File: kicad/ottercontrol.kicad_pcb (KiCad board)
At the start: 2 copper layers, 97.8 x 52.1 mm, 114 parts, among them IC1 MAX485, IC2 USBLC6-4, IC3 USBLC6-2SC6, J1 USB_B_Micro, P1 Conn_01x02, Q1 Q_PMOS_GSD, Q2 IRF3205, Q3 IRF3205, Q4 IRF3205, Q5 IRF3205, Q6 IRF3205, Q7 IRF3205, U1 STM32F303CBT6, U2 MAX3051, U3 MIC4605, U4 MIC4605, U5 MIC4605, U6 XL7015, U7 ACT4088, U8 MIC5504-3.3YM5, X1 programmer, X2 Conn_01x08, X3 Conn_01x05, Y1 16MHz

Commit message: placed and routed; preliminary finished
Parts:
- added GND1: Conn_01x01, TestPoint:TestPoint_THTPad_4.0x4.0mm_Drill2.0mm, F.Cu at (140.3, 80.0)
- added R48: 0, Resistor_SMD:R_0603_1608Metric, F.Cu at (134.0, 69.2)
- added VDC1: Conn_01x01, TestPoint:TestPoint_THTPad_4.0x4.0mm_Drill2.0mm, F.Cu at (62.9, 80.0)
- added VDC2: Conn_01x01, TestPoint:TestPoint_THTPad_4.0x4.0mm_Drill2.0mm, F.Cu at (57.1, 80.0)
- X1: footprint Connector_PinHeader_2.54mm:PinHeader_2x03_P2.54mm_Vertical -> Connector:Tag-Connect_TC2030-IDC-NL_2x03_P1.27mm_Vertical
- X2: footprint Connector_JST:JST_GH_SM08B-GHS-TB_1x08-1MP_P1.25mm_Horizontal -> Connector_Molex:Molex_PicoBlade_53261-0871_1x08-1MP_P1.25mm_Horizontal
- X3: footprint Connector_JST:JST_GH_SM05B-GHS-TB_1x05-1MP_P1.25mm_Horizontal -> Connector_Molex:Molex_PicoBlade_53261-0571_1x05-1MP_P1.25mm_Horizontal
- moved C3 25.6 mm to (116.2, 66.0), turned to 90 degrees
- moved C11 12.1 mm to (104.8, 64.8), turned to 270 degrees
- moved C12 11.5 mm to (94.0, 64.8), turned to 270 degrees
- moved C13 10.9 mm to (83.2, 64.8), turned to 270 degrees
- moved R27 6.29 mm to (89.5, 47.6)
- moved R43 5.99 mm to (108.0, 73.0)
- moved X2 5.99 mm to (91.4, 81.9)
- moved R14 5.85 mm to (119.4, 79.4)
- moved R3 5.85 mm to (119.4, 81.9)
- moved X3 5.46 mm to (107.3, 81.9)
- moved LED1 5.46 mm to (117.5, 81.9)
- moved R2 5.12 mm to (115.6, 81.9), turned to 270 degrees
- moved R11 5.12 mm to (120.7, 78.1)
- moved U2 4.96 mm to (95.2, 74.3)
- moved IC1 4.96 mm to (88.9, 74.3)
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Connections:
- net Net-(R15-Pad2) renamed /Phase Driver 1/HO
- net Net-(R16-Pad2) renamed /Phase Driver 2/HO
- net Net-(R17-Pad2) renamed /Phase Driver 3/HO
- net Net-(R18-Pad2) renamed /Phase Driver 1/LO
- net Net-(R19-Pad2) renamed /Phase Driver 2/LO
- net Net-(R20-Pad2) renamed /Phase Driver 3/LO
- C5 pad 1: +5V -> +3V3
- IC1 pad 4: /RS458_TX -> /RS485_TX
- IC2 pad 5: +3V3 -> +5V
- IC3 pad 4: Net-(IC3-Pad4) -> Net-(IC3-Pad3)
- IC3 pad 6: Net-(IC3-Pad6) -> Net-(IC3-Pad1)
- R11 pad 1: Net-(IC3-Pad6) -> Net-(IC3-Pad1)
- R12 pad 2: Net-(IC3-Pad4) -> Net-(IC3-Pad3)
- R14 pad 2: Net-(IC3-Pad4) -> Net-(IC3-Pad3)
- U1 pad 21: /RS458_TX -> /RS485_TX
- U2 pad 3: +5V -> +3V3
- X3 pad 5: +3V3 -> +5V
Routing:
- net +12V: track 0.00 -> 67.1 mm, vias 0 -> 9
- net +5V: track 0.00 -> 66.8 mm
- net +3V3: track 0.00 -> 66.0 mm, vias 0 -> 18
- net /VSENS3: track 0.00 -> 52.0 mm, vias 0 -> 2
- net GND: track 0.00 -> 48.3 mm, vias 0 -> 26
- net /RS485_RX: track 0.00 -> 43.9 mm, vias 0 -> 2
- net Net-(Q7-Pad3): track 0.00 -> 41.3 mm, vias 0 -> 3
- net /RS485_DE: track 0.00 -> 40.7 mm, vias 0 -> 2
- net /Phase Driver 1/PHASE: track 0.00 -> 40.1 mm, vias 0 -> 74
- net /CAN_EN: track 0.00 -> 39.5 mm, vias 0 -> 2
- net /CAN_TX: track 0.00 -> 39.3 mm, vias 0 -> 3
- net /VSENS1: track 0.00 -> 39.1 mm, vias 0 -> 3
- net /PWML3: track 0.00 -> 37.6 mm, vias 0 -> 2
- net +VDC: track 0.00 -> 37.6 mm, vias 0 -> 74
- net /VSENS2: track 0.00 -> 37.5 mm, vias 0 -> 3
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- added copper zone on F.Cu, net +12V
- added copper zone on In1.Cu, net +12V
- added copper zone on In1.Cu, net +3V3
- added copper zone on B.Cu, net +VDC
- added copper zone on F.Cu, net +VDC
- added copper zone on In1.Cu, net +VDC
- added copper zone on B.Cu, net /Phase Driver 1/PHASE
- added copper zone on F.Cu, net /Phase Driver 1/PHASE
- added copper zone on B.Cu, net /Phase Driver 2/PHASE
- added copper zone on F.Cu, net /Phase Driver 2/PHASE
- added copper zone on B.Cu, net /Phase Driver 3/PHASE
- added copper zone on F.Cu, net /Phase Driver 3/PHASE
- added copper zone on F.Cu, net GND
- added copper zone on In2.Cu, net GND
- added copper zone on B.Cu, net GNDPWR
- added copper zone on F.Cu, net GNDPWR
- added copper zone on In2.Cu, net GNDPWR
- added copper zone on F.Cu, net Net-(D9-Pad1)
- added copper zone on F.Cu, net Net-(Q5-Pad3)
- added copper zone on F.Cu, net Net-(Q6-Pad3)
- added copper zone on F.Cu, net Net-(Q7-Pad3)
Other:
- board size 97.8 x 52.1 mm -> 94 x 47 mm
- copper layers 2 -> 4
- net class 0.3mm added: clearance 0.2, trace_width 0.3, via_dia 0.8, via_drill 0.4
- net class 0.5mm added: clearance 0.2, trace_width 0.5, via_dia 0.8, via_drill 0.4
- net class 0.6mm added: clearance 0.2, trace_width 0.6, via_dia 0.8, via_drill 0.4
- net class 1.0mm added: clearance 0.2, trace_width 1, via_dia 1, via_drill 0.5
- net class Default: trace_width 0.25 -> 0.15; via_dia 0.8 -> 0.5; via_drill 0.4 -> 0.3
- net class High Power added: clearance 0.2, trace_width 0.8, via_dia 0.8, via_drill 0.4
- rule trace_min: 0.2 -> 0.15
- rule via_min_drill: 0.3 -> 0.25
- rule via_min_size: 0.4 -> 0.5

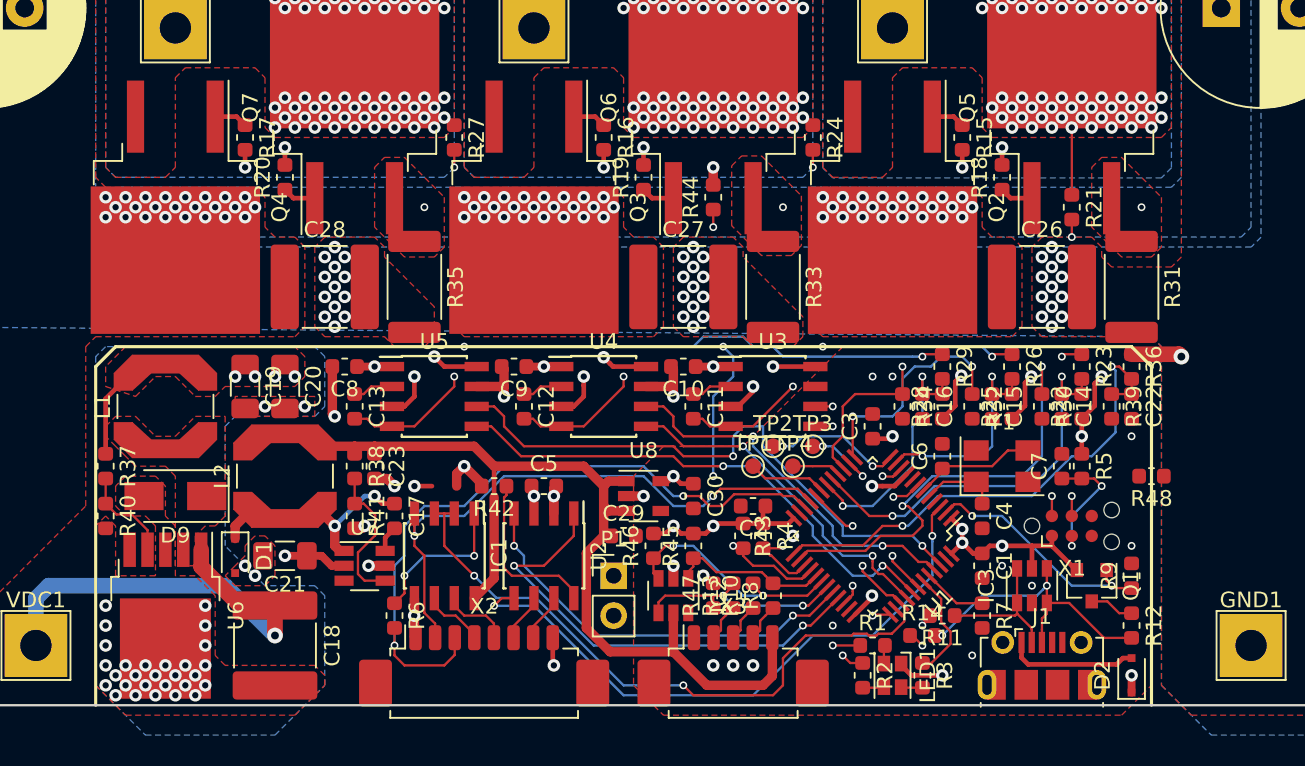
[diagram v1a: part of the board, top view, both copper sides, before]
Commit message: made footprint fot mosfets hybrid for TO220 and D2PAK; added jumper instead of 0 Ohm resistor
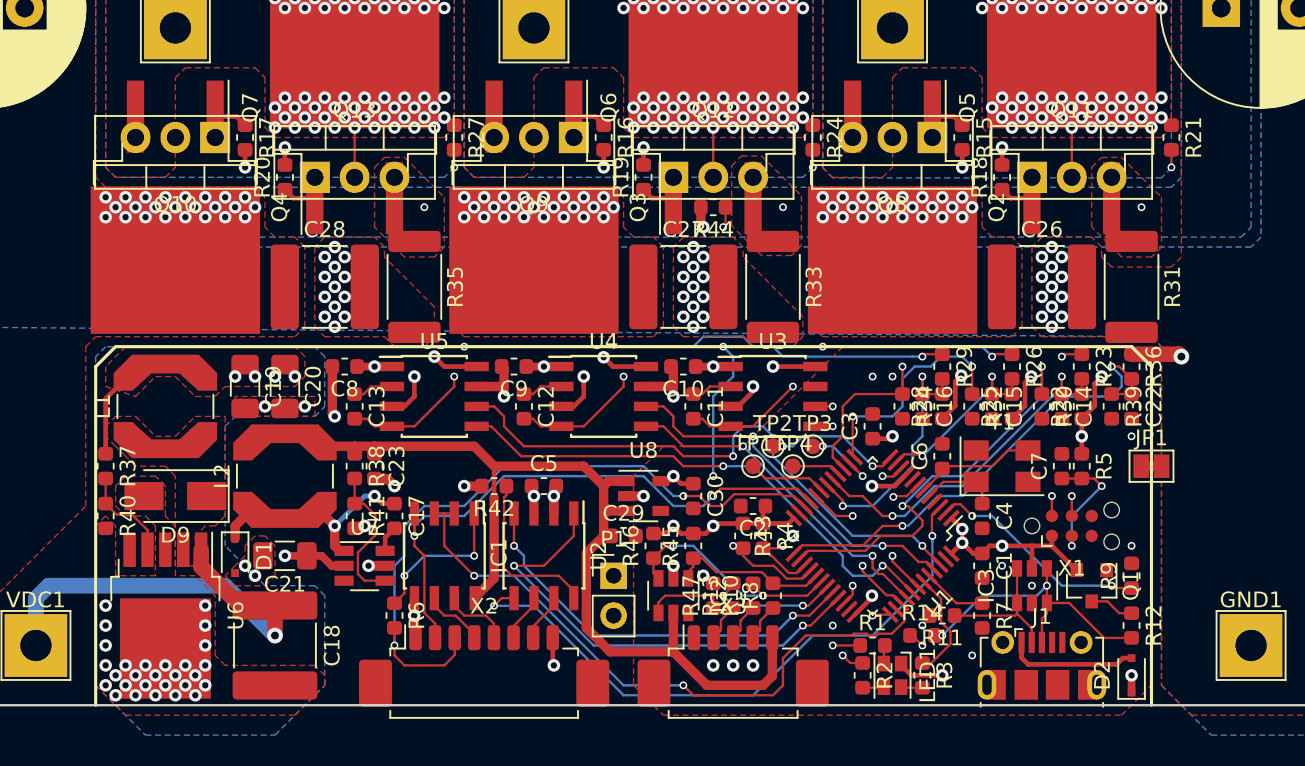
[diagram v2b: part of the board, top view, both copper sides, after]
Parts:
- removed R48: 0, Resistor_SMD:R_0603_1608Metric
- added JP1: GND Bridge, Jumper:SolderJumper-2_P1.3mm_Bridged_Pad1.0x1.5mm, F.Cu at (134.0, 68.6)
- added Q10: IRF3205, Package_TO_SOT_THT:TO-220-3_Vertical, F.Cu at (74.3, 47.6)
- added Q11: IRF3205, Package_TO_SOT_THT:TO-220-3_Vertical, F.Cu at (126.4, 50.2)
- added Q12: IRF3205, Package_TO_SOT_THT:TO-220-3_Vertical, F.Cu at (103.5, 50.2)
- added Q13: IRF3205, Package_TO_SOT_THT:TO-220-3_Vertical, F.Cu at (80.6, 50.2)
- added Q8: IRF3205, Package_TO_SOT_THT:TO-220-3_Vertical, F.Cu at (120.0, 47.6)
- added Q9: IRF3205, Package_TO_SOT_THT:TO-220-3_Vertical, F.Cu at (97.2, 47.6)
- C24, C25: value 10u -> 100u
- C29: value 10u -> 1u
- C3: value 100n -> 10u
- R12: value 1.5 -> 1.5k
- moved R21 7.75 mm to (135.3, 47.6)
- moved R44 0.63 mm to (106.0, 52.1), turned to 180 degrees
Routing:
- net +3V3: track 66.0 -> 57.0 mm, vias 18 -> 17
- net /VSENS1: track 39.1 -> 44.5 mm
- net GND: track 48.3 -> 42.9 mm
- net /ISENS1: track 25.6 -> 23.0 mm
- net /Phase Driver 1/PHASE: track 40.1 -> 37.6 mm
- net /ISENS2: track 14.5 -> 12.2 mm
- net /Phase Driver 2/PHASE: track 26.3 -> 28.1 mm
- net Net-(R1-Pad1): track 16.6 -> 18.2 mm
- net /Phase Driver 3/PHASE: track 28.3 -> 26.7 mm
- net /Phase Driver 3/LO: track 21.7 -> 23.2 mm
- net /VSENSBUS: track 31.8 -> 30.7 mm

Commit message: added finished adding MPNs to all components
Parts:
- removed GND1, PHASE1, PHASE2, PHASE3, VDC1, VDC2: Conn_01x01, TestPoint:TestPoint_THTPad_4.0x4.0mm_Drill2.0mm
- removed X1: programmer, Connector:Tag-Connect_TC2030-IDC-NL_2x03_P1.27mm_Vertical
- removed X2: Conn_01x08, Connector_Molex:Molex_PicoBlade_53261-0871_1x08-1MP_P1.25mm_Horizontal
- removed X3: Conn_01x05, Connector_Molex:Molex_PicoBlade_53261-0571_1x05-1MP_P1.25mm_Horizontal
- added P2: Conn_01x08, Connector_Molex:Molex_PicoBlade_53261-0871_1x08-1MP_P1.25mm_Horizontal, F.Cu at (91.4, 81.9)
- added P3: Conn_01x05, Connector_Molex:Molex_PicoBlade_53261-0571_1x05-1MP_P1.25mm_Horizontal, F.Cu at (107.3, 81.9)
- added P4: Conn_01x02, Connector_PinHeader_2.54mm:PinHeader_1x02_P2.54mm_Vertical, F.Cu at (99.7, 75.6)
- added PAD1: Conn_01x01, TestPoint:TestPoint_THTPad_4.0x4.0mm_Drill2.0mm, F.Cu at (117.5, 40.0)
- added PAD2: Conn_01x01, TestPoint:TestPoint_THTPad_4.0x4.0mm_Drill2.0mm, F.Cu at (94.6, 40.0)
- added PAD3: Conn_01x01, TestPoint:TestPoint_THTPad_4.0x4.0mm_Drill2.0mm, F.Cu at (71.8, 40.0)
- added PAD4: Conn_01x01, TestPoint:TestPoint_THTPad_4.0x4.0mm_Drill2.0mm, F.Cu at (57.1, 80.0)
- added PAD5: Conn_01x01, TestPoint:TestPoint_THTPad_4.0x4.0mm_Drill2.0mm, F.Cu at (62.9, 80.0)
- added PAD6: Conn_01x01, TestPoint:TestPoint_THTPad_4.0x4.0mm_Drill2.0mm, F.Cu at (141.0, 80.0)
- P1: value Conn_01x02 -> programmer; footprint Connector_PinHeader_2.54mm:PinHeader_1x02_P2.54mm_Vertical -> Connector:Tag-Connect_TC2030-IDC-NL_2x03_P1.27mm_Vertical
- Q1: value Q_PMOS_GSD -> Si2367DS
- Q10, Q11, Q12, Q13, Q8, Q9: value IRF3205 -> IRF100B201
- Q2, Q3, Q4, Q5, Q6, Q7: value IRF3205 -> TK160F10N1L
- Y1: footprint Crystal:Crystal_SMD_5032-4Pin_5.0x3.2mm -> Crystal:Crystal_SMD_3225-4Pin_3.2x2.5mm
- moved P1 29.4 mm to (128.9, 72.4)
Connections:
- P1 pad 1: /TMP_M -> +3V3
- P1 pad 2: GND -> /SWDIO
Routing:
- net Net-(C4-Pad1): track 4.92 -> 5.59 mm

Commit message: finalyzed design
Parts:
- added D3: 1N4148, Diode_SMD:D_SOD-323F, F.Cu at (67.3, 43.8)
- added D4: 1N4148, Diode_SMD:D_SOD-323F, F.Cu at (55.9, 43.8)
- added D5: 1N4148, Diode_SMD:D_SOD-323F, F.Cu at (44.5, 43.8)
- added REF**: KiCAD Logo, Symbol:Symbol_KiCAD-Logo_CopperAndSilkScreenTop, B.Cu at (21.6, 44.5)
- C11, C12, C13: value 1u -> 2.2u
- IC3: value USBLC6-2SC6 -> USBLC6-4
- LED1: value CLMVB-FKA -> LED_RABG; footprint LED_SMD:LED_Cree-PLCC4_2x2mm_CW -> LED_SMD:LED_Avago_PLCC4_3.2x2.8mm_CW
- U3, U4, U5: value MIC4605 -> IR2102
- moved R2 44.3 mm to (76.8, 60.3)
- moved C13 44.2 mm to (45.7, 41.3), turned to 90 degrees
- moved R1 44.1 mm to (78.1, 57.8)
- moved U5 44.1 mm to (50.2, 41.9), turned to 180 degrees
- moved C3 43.9 mm to (78.7, 43.2)
- moved D2 43.8 mm to (94.6, 60.3)
- moved IC1 43.8 mm to (50.8, 52.7)
- moved Q1 43.8 mm to (92.1, 54.6)
- moved R11 43.8 mm to (82.5, 56.5)
- moved R43 43.8 mm to (69.8, 51.4)
- moved TP2 43.8 mm to (71.8, 45.7)
- moved C14 43.8 mm to (90.2, 43.2)
- moved C15 43.8 mm to (85.7, 43.2)
- moved C18 43.8 mm to (40.0, 58.4)
- moved C19 43.8 mm to (38.1, 41.9)
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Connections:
- C10 pad 2: GND -> GNDPWR
- C8 pad 2: GND -> GNDPWR
- C9 pad 2: GND -> GNDPWR
- LED1 pad 1: +3V3 -> Net-(LED1-Pad1)
- LED1 pad 2: Net-(LED1-Pad2) -> +3V3
- R1 pad 2: Net-(LED1-Pad4) -> Net-(LED1-Pad1)
- R2 pad 2: Net-(LED1-Pad3) -> Net-(LED1-Pad4)
- R3 pad 2: Net-(LED1-Pad2) -> Net-(LED1-Pad3)
- U3 pad 2: Net-(C11-Pad1) -> /PWMH1
- U3 pad 3: /Phase Driver 1/HO -> /PWML1
- U3 pad 4: /Phase Driver 1/PHASE -> GNDPWR
- U3 pad 5: /PWMH1 -> /Phase Driver 1/LO
- U3 pad 6: /PWML1 -> /Phase Driver 1/PHASE
- U3 pad 7: GND -> /Phase Driver 1/HO
- U3 pad 8: /Phase Driver 1/LO -> Net-(C11-Pad1)
- U4 pad 2: Net-(C12-Pad1) -> /PWMH2
- U4 pad 3: /Phase Driver 2/HO -> /PWML2
- U4 pad 4: /Phase Driver 2/PHASE -> GNDPWR
- U4 pad 5: /PWMH2 -> /Phase Driver 2/LO
- U4 pad 6: /PWML2 -> /Phase Driver 2/PHASE
- U4 pad 7: GND -> /Phase Driver 2/HO
- U4 pad 8: /Phase Driver 2/LO -> Net-(C12-Pad1)
- U5 pad 2: Net-(C13-Pad1) -> /PWMH3
- U5 pad 3: /Phase Driver 3/HO -> /PWML3
- U5 pad 4: /Phase Driver 3/PHASE -> GNDPWR
- U5 pad 5: /PWMH3 -> /Phase Driver 3/LO
- U5 pad 6: /PWML3 -> /Phase Driver 3/PHASE
- U5 pad 7: GND -> /Phase Driver 3/HO
- U5 pad 8: /Phase Driver 3/LO -> Net-(C13-Pad1)
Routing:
- net GND: track 42.9 -> 27.6 mm, vias 26 -> 22
- net +12V: track 67.1 -> 77.6 mm
- net GNDPWR: track 1.91 -> 11.1 mm, vias 69 -> 72
- net /PWMH1: track 14.5 -> 23.0 mm
- net /PWML1: track 14.9 -> 21.0 mm
- net /Phase Driver 1/PHASE: track 37.6 -> 32.6 mm
- net /VSENS2: track 37.5 -> 33.2 mm
- net /SWDIO: track 19.2 -> 23.4 mm
- net /PWML2: track 23.5 -> 27.2 mm
- net /PWMH3: track 33.1 -> 36.5 mm
- net /VSENS3: track 52.0 -> 48.6 mm, vias 2 -> 3
- net Net-(Q12-Pad3): track 22.3 -> 19.0 mm
- net Net-(R1-Pad1): track 18.2 -> 15.0 mm
- net /PWMH2: track 21.6 -> 24.4 mm
- net /PWML3: track 37.2 -> 39.9 mm
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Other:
- outline, holes or cut-outs redrawn
- board text added: "3.3V CANH CANL 485A 485B RX TX GND"
- board text added: "5V PA8 PA9 PA10 GND"
- board text added: "GND"
- board text added: "MULTICOM"
- board text added: "OtterControl v0.1k"
- board text added: "SENSOR"
- board text added: "U"
- board text added: "V"
- board text added: "VBAT"
- board text added: "W"
